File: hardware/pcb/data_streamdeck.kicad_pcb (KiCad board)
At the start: 2 copper layers, 55 x 112 mm, 49 parts, among them J1 ScreenKey 1, J2 ScreenKey 2, J3 ScreenKey 3, J4 ScreenKey 4, J5 ScreenKey 5, J6 ScreenKey 6, J7 USB4105-GF-A, J8 microSD, SW1 BOOT, SW2 RESET, U1 ESP32-S3-WROOM-1-N16R8, U2 AMS1117-3.3, U3 USBLC6-2SC6

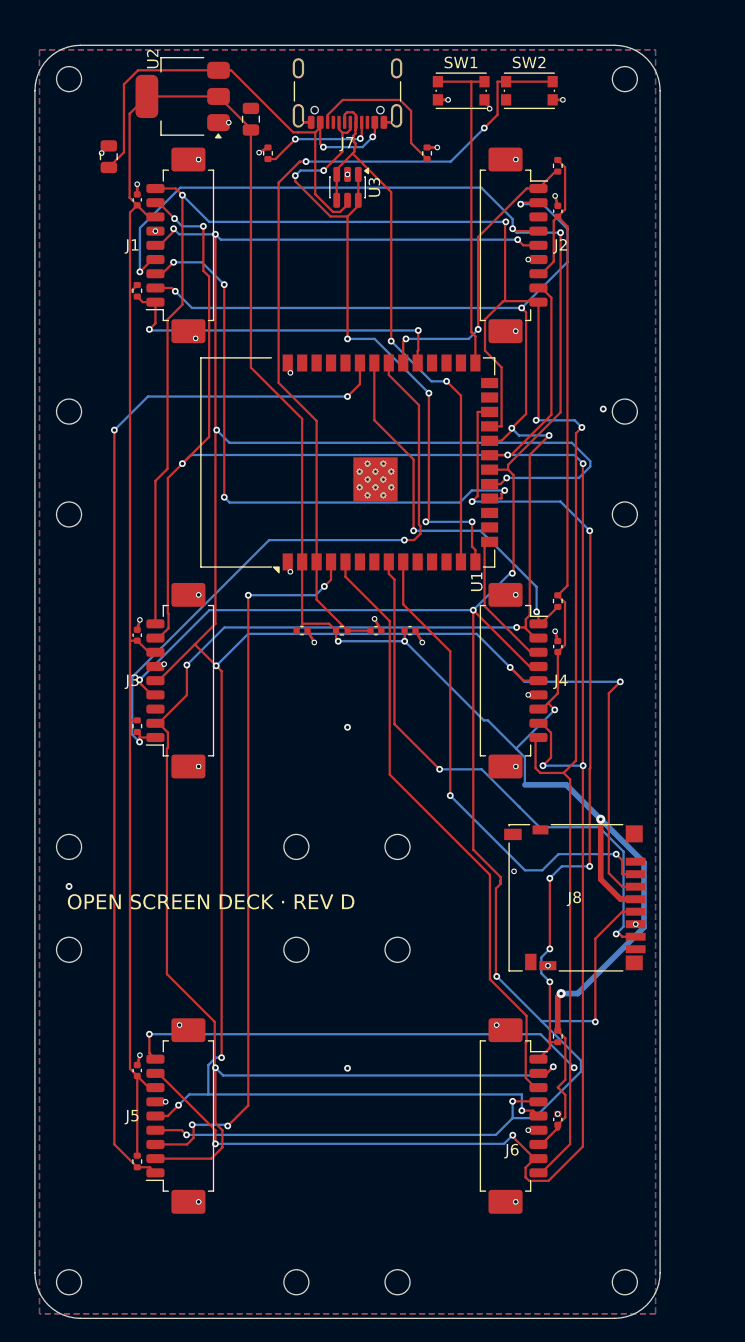
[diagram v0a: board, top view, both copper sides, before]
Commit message: Rev E hardware, firmware 0.14.5, and docs for sensors and glow
Ship the dual-SPI carrier with IMU, ambient light, haptics, SK6812 edge
LEDs and Qwiic, plus companion flash overlay and GitHub Pages that match
the board.

Co-authored-by: Cursor <cursoragent@cursor.com>
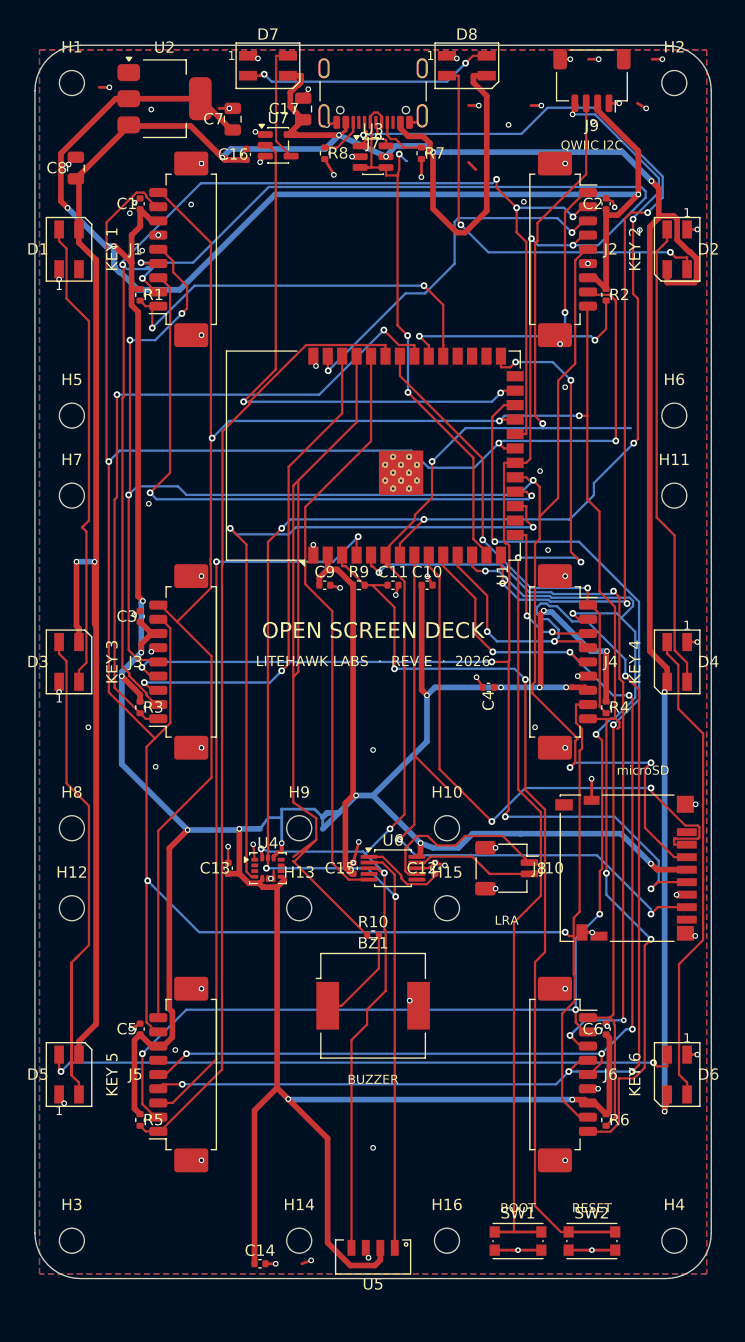
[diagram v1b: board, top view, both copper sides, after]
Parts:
- added BZ1: CPT-9019S, Buzzer_Beeper:Buzzer_CUI_CPT-9019S-SMT, F.Cu at (29.8, 84.5)
- added C12: 1uF, Capacitor_SMD:C_0402_1005Metric, F.Cu at (35.2, 72.4)
- added C13: 100nF, Capacitor_SMD:C_0402_1005Metric, F.Cu at (17.0, 72.4)
- added C14: 100nF, Capacitor_SMD:C_0402_1005Metric, F.Cu at (19.8, 107.2)
- added C15: 100nF, Capacitor_SMD:C_0402_1005Metric, F.Cu at (28.0, 72.4)
- added C16: 100nF, Capacitor_SMD:C_0402_1005Metric, F.Cu at (18.6, 9.60)
- added C17: 10uF, Capacitor_SMD:C_0805_2012Metric, F.Cu at (23.6, 5.60)
- added D1: SK6812MINI-E, LED_SMD:LED_SK6812MINI_PLCC4_3.5x3.5mm_P1.75mm, F.Cu at (3.00, 17.9)
- added D2: SK6812MINI-E, LED_SMD:LED_SK6812MINI_PLCC4_3.5x3.5mm_P1.75mm, F.Cu at (56.5, 17.9)
- added D3: SK6812MINI-E, LED_SMD:LED_SK6812MINI_PLCC4_3.5x3.5mm_P1.75mm, F.Cu at (3.00, 54.2)
- added D4: SK6812MINI-E, LED_SMD:LED_SK6812MINI_PLCC4_3.5x3.5mm_P1.75mm, F.Cu at (56.5, 54.2)
- added D5: SK6812MINI-E, LED_SMD:LED_SK6812MINI_PLCC4_3.5x3.5mm_P1.75mm, F.Cu at (3.00, 90.5)
- added D6: SK6812MINI-E, LED_SMD:LED_SK6812MINI_PLCC4_3.5x3.5mm_P1.75mm, F.Cu at (56.5, 90.5)
- added D7: SK6812MINI-E, LED_SMD:LED_SK6812MINI_PLCC4_3.5x3.5mm_P1.75mm, F.Cu at (20.5, 1.80)
- added D8: SK6812MINI-E, LED_SMD:LED_SK6812MINI_PLCC4_3.5x3.5mm_P1.75mm, F.Cu at (38.0, 1.80)
- added J10: LRA motor, Connector_JST:JST_SH_SM02B-SRSS-TB_1x02-1MP_P1.00mm_Horizontal, F.Cu at (41.5, 72.4)
- added J9: Qwiic, Connector_JST:JST_SH_SM04B-SRSS-TB_1x04-1MP_P1.00mm_Horizontal, F.Cu at (49.0, 3.10)
- added R10: 100R, Resistor_SMD:R_0402_1005Metric, F.Cu at (29.8, 78.3)
- added U4: LSM6DS3TR-C, Package_LGA:LGA-14_3x2.5mm_P0.5mm_LayoutBorder3x4y, F.Cu at (20.5, 72.4)
- added U5: VEML7700, OpenScreenDeck:VEML7700-TT, F.Cu at (29.8, 106.6)
- added U6: DRV2605L, Package_SO:MSOP-10_3x3mm_P0.5mm, F.Cu at (31.5, 72.4)
- added U7: 74AHCT1G125, Package_TO_SOT_SMD:SOT-23-5, F.Cu at (21.4, 8.80)
- moved SW2 101.3 mm to (49.0, 105.2)
- moved SW1 101.3 mm to (42.5, 105.2)
- moved R7 13.5 mm to (34.0, 9.50), turned to -90 degrees
- moved R2 12.1 mm to (50.2, 21.9)
- moved R4 10.3 mm to (50.2, 58.2)
- moved C6 9.01 mm to (50.2, 86.5)
- moved R8 9.00 mm to (25.5, 9.50), turned to -90 degrees
- moved R6 8.49 mm to (50.2, 94.5)
- moved C4 7.08 mm to (39.9, 56.5), turned to 180 degrees
- moved H15 5.68 mm to (36.2, 75.9)
- moved H16 5.68 mm to (36.2, 105.2)
- moved H4 5.68 mm to (56.2, 105.2)
- moved J6 5.68 mm to (46.2, 90.5)
- moved J8 5.20 mm to (52.0, 72.4)
- moved H11 4.65 mm to (56.2, 39.6)
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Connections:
- J1 pad 2: DC -> DC_A
- J1 pad 4: SCK -> SCK_A
- J1 pad 5: MOSI -> MOSI_A
- J2 pad 2: DC -> DC_A
- J2 pad 4: SCK -> SCK_A
- J2 pad 5: MOSI -> MOSI_A
- J3 pad 2: DC -> DC_A
- J3 pad 4: SCK -> SCK_A
- J3 pad 5: MOSI -> MOSI_A
- J4 pad 2: DC -> DC_B
- J4 pad 4: SCK -> SCK_B
- J4 pad 5: MOSI -> MOSI_B
- J5 pad 2: DC -> DC_B
- J5 pad 4: SCK -> SCK_B
- J5 pad 5: MOSI -> MOSI_B
- J6 pad 2: DC -> DC_B
- J6 pad 4: SCK -> SCK_B
- J6 pad 5: MOSI -> MOSI_B
- J8 pad 3: MOSI -> MOSI_A
- J8 pad 5: SCK -> SCK_A
- U1 pad 10: (no net) -> MOSI_B
- U1 pad 11: (no net) -> SCK_B
- U1 pad 12: (no net) -> DC_B
- U1 pad 17: (no net) -> IMU_INT
- U1 pad 19: MOSI -> MOSI_A
- U1 pad 20: SCK -> SCK_A
- U1 pad 22: DC -> DC_A
- U1 pad 25: (no net) -> LED_DATA_3V3
- U1 pad 36: (no net) -> HAPTIC_EN
- U1 pad 37: (no net) -> PIEZO
- U1 pad 38: (no net) -> CS3
- U1 pad 39: (no net) -> CS2
- U1 pad 6: (no net) -> SDA
- U1 pad 7: (no net) -> SCL
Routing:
- net MOSI: track 259.8 -> 0.00 mm, vias 11 -> 0
- net VBUS: track 46.2 -> 292.7 mm, vias 2 -> 9
- net SCK: track 234.4 -> 0.00 mm, vias 10 -> 0
- net DC: track 200.4 -> 0.00 mm, vias 9 -> 0
- net SCK_A: track 0.00 -> 172.0 mm, vias 0 -> 7
- net SCL: track 0.00 -> 153.2 mm, vias 0 -> 7
- net MOSI_A: track 0.00 -> 152.4 mm, vias 0 -> 6
- net +3V3: track 303.5 -> 450.4 mm, vias 5 -> 20
- net SDA: track 0.00 -> 137.8 mm, vias 0 -> 5
- net DC_A: track 0.00 -> 114.7 mm, vias 0 -> 5
- net SCK_B: track 0.00 -> 112.9 mm, vias 0 -> 6
- net DC_B: track 0.00 -> 110.6 mm, vias 0 -> 6
- net MOSI_B: track 0.00 -> 101.1 mm, vias 0 -> 6
- net PIEZO: track 0.00 -> 77.9 mm
- net BOOT: track 29.0 -> 95.2 mm, vias 0 -> 4
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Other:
- board size 55 x 112 mm -> 59.5 x 108.5 mm
- board text added: "BOOT"
- board text added: "BUZZER"
- board text added: "KEY 1"
- board text added: "KEY 2"
- board text added: "KEY 3"
- board text added: "KEY 4"
- board text added: "KEY 5"
- board text added: "KEY 6"
- board text added: "LITEHAWK LABS · REV E · 2026"
- board text added: "LRA"
- board text added: "OPEN SCREEN DECK · REV E"
- board text added: "QWIIC I2C"
- board text added: "RESET"
- board text added: "microSD"
- board text removed: "OPEN SCREEN DECK · REV D"
- board text removed: "REV D · 2026"
